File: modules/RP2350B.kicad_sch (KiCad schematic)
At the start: 34 parts, among them SW1 SW_Push, SW2 SW_Push, U1 RP2350B, U5 W25Q128JVS, U6 W25Q128JVS, Y1 12MHz

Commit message: Adding source, source control
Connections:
- net RP_NRESET: now reaches SW1.2, U1.35 (RUN)
- net RPB_CLK renamed RPB_SPI_CLK
- net RPB_MISO renamed RPB_SPI_MISO
- net RPB_MOSI renamed RPB_SPI_MOSI
- net RPB_SS renamed RPB_SPI_SS
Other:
- moved on the sheet: R7, SW1
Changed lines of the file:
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@@
 	(wire
 		(pts
-			(xy 64.77 130.81) (xy 64.77 132.08)
+			(xy 58.42 130.81) (xy 58.42 132.08)
 		)
 		(stroke
@@
 	(wire
 		(pts
-			(xy 88.9 130.81) (xy 100.33 130.81)
+			(xy 82.55 130.81) (xy 100.33 130.81)
 		)
 		(stroke
@@
 	(wire
 		(pts
-			(xy 71.12 130.81) (xy 64.77 130.81)
+			(xy 64.77 130.81) (xy 58.42 130.81)
 		)
 		(stroke
@@
 		)
 	)
+	(label "RP_NRESET"
+		(at 83.82 130.81 0)
+		(effects
+			(font
+				(size 1.27 1.27)
+			)
+			(justify left bottom)
+		)
+	)
 	(label "QSPI_SD2"
 		(at 210.82 132.08 0)
@@
 		)
 	)
+	(hierarchical_label "RPB_SWO"
+		(shape output)
+		(at 38.1 179.07 0)
+		(effects
+			(font
+				(size 1.27 1.27)
+			)
+			(justify left)
+		)
+	)
 	(hierarchical_label "USB_DM"
 		(shape input)
@@
 		)
 	)
-	(hierarchical_label "RPB_CLK"
+	(hierarchical_label "RPB_SPI_CLK"
 		(shape output)
 		(at 160.02 69.85 0)
@@
 		)
 	)
-	(hierarchical_label "RPB_SS"
+	(hierarchical_label "RPB_SPI_SS"
 		(shape output)
 		(at 160.02 72.39 0)
@@
 		)
 	)
-	(hierarchical_label "RPB_MOSI"
+	(hierarchical_label "RPB_SPI_MOSI"
 		(shape input)
 		(at 160.02 67.31 0)
@@
 		)
 	)
-	(hierarchical_label "RPB_MISO"
+	(hierarchical_label "RPB_SPI_MISO"
 		(shape output)
 		(at 160.02 64.77 0)
@@
 		)
 	)
+	(hierarchical_label "RPB_I2C_SDA"
+		(shape output)
+		(at 38.1 182.88 0)
+		(effects
+			(font
+				(size 1.27 1.27)
+			)
+			(justify left)
+		)
+	)
+	(hierarchical_label "RPB_I2C_SCL"
+		(shape output)
+		(at 38.1 186.69 0)
+		(effects
+			(font
+				(size 1.27 1.27)
+			)
+			(justify left)
+		)
+	)
 	(symbol
 		(lib_id "Device:C")
@@
 	(symbol
 		(lib_id "power:GND")
-		(at 64.77 132.08 0)
+		(at 58.42 132.08 0)
 		(unit 1)
 		(exclude_from_sim no)
@@
 		(fields_autoplaced yes)
 		(property "Reference" "#PWR018"
-			(at 64.77 138.43 0)
+			(at 58.42 138.43 0)
 			(effects
 				(font
@@
 		)
 		(property "Value" "GND"
-			(at 64.77 137.16 0)
+			(at 58.42 137.16 0)
 			(effects
 				(font
@@
 		)
 		(property "Footprint" ""
-			(at 64.77 132.08 0)
+			(at 58.42 132.08 0)
 			(effects
 				(font
@@
 		)
 		(property "Datasheet" ""
-			(at 64.77 132.08 0)
+			(at 58.42 132.08 0)
 			(effects
 				(font
@@
 		)
 		(property "Description" "Power symbol creates a global label with name \"GND\" , ground"
-			(at 64.77 132.08 0)
+			(at 58.42 132.08 0)
 			(effects
 				(font
@@
 	(symbol
 		(lib_id "Device:R")
-		(at 74.93 130.81 90)
+		(at 68.58 130.81 90)
 		(unit 1)
 		(exclude_from_sim no)
@@
 		(dnp no)
 		(property "Reference" "R7"
-			(at 74.93 128.778 90)
+			(at 68.58 128.778 90)
 			(effects
 				(font
@@
 		)
 		(property "Value" "1K"
-			(at 74.93 133.096 90)
+			(at 68.58 133.096 90)
 			(effects
 				(font
@@
 		)
 		(property "Footprint" "Resistor_SMD:R_0402_1005Metric"
-			(at 74.93 132.588 90)
+			(at 68.58 132.588 90)
 			(effects
 				(font
@@
 		)
 		(property "Datasheet" "https://industrial.panasonic.com/cdbs/www-data/pdf/RDA0000/AOA0000C304.pdf"
-			(at 74.93 130.81 0)
+			(at 68.58 130.81 0)
 			(effects
 				(font
@@
 		)
 		(property "Description" "RES SMD 1K OHM 1% 1/10W 0402"
-			(at 74.93 130.81 0)
+			(at 68.58 130.81 0)
 			(effects
 				(font
@@
 		)
 		(property "Part Number" "ERJ-2RKF1001X"
-			(at 74.93 130.81 90)
+			(at 68.58 130.81 90)
 			(effects
 				(font
@@
 		)
 		(property "Provider" "Digikey"
-			(at 74.93 130.81 90)
+			(at 68.58 130.81 90)
 			(effects
 				(font
@@
 	(symbol
 		(lib_id "Switch:SW_Push")
-		(at 83.82 130.81 0)
+		(at 77.47 130.81 0)
 		(unit 1)
 		(exclude_from_sim no)
@@
 		(fields_autoplaced yes)
 		(property "Reference" "SW1"
-			(at 83.82 123.19 0)
+			(at 77.47 123.19 0)
 			(effects
 				(font
@@
 		)
 		(property "Value" "SW_Push"
-			(at 83.82 125.73 0)
+			(at 77.47 125.73 0)
 			(effects
 				(font
@@
 		)
 		(property "Footprint" ""
-			(at 83.82 125.73 0)
+			(at 77.47 125.73 0)
 			(effects
 				(font
@@
 		)
 		(property "Datasheet" "~"
-			(at 83.82 125.73 0)
+			(at 77.47 125.73 0)
 			(effects
 				(font
@@
 		)
 		(property "Description" "Push button switch, generic, two pins"
-			(at 83.82 130.81 0)
+			(at 77.47 130.81 0)
 			(effects
 				(font

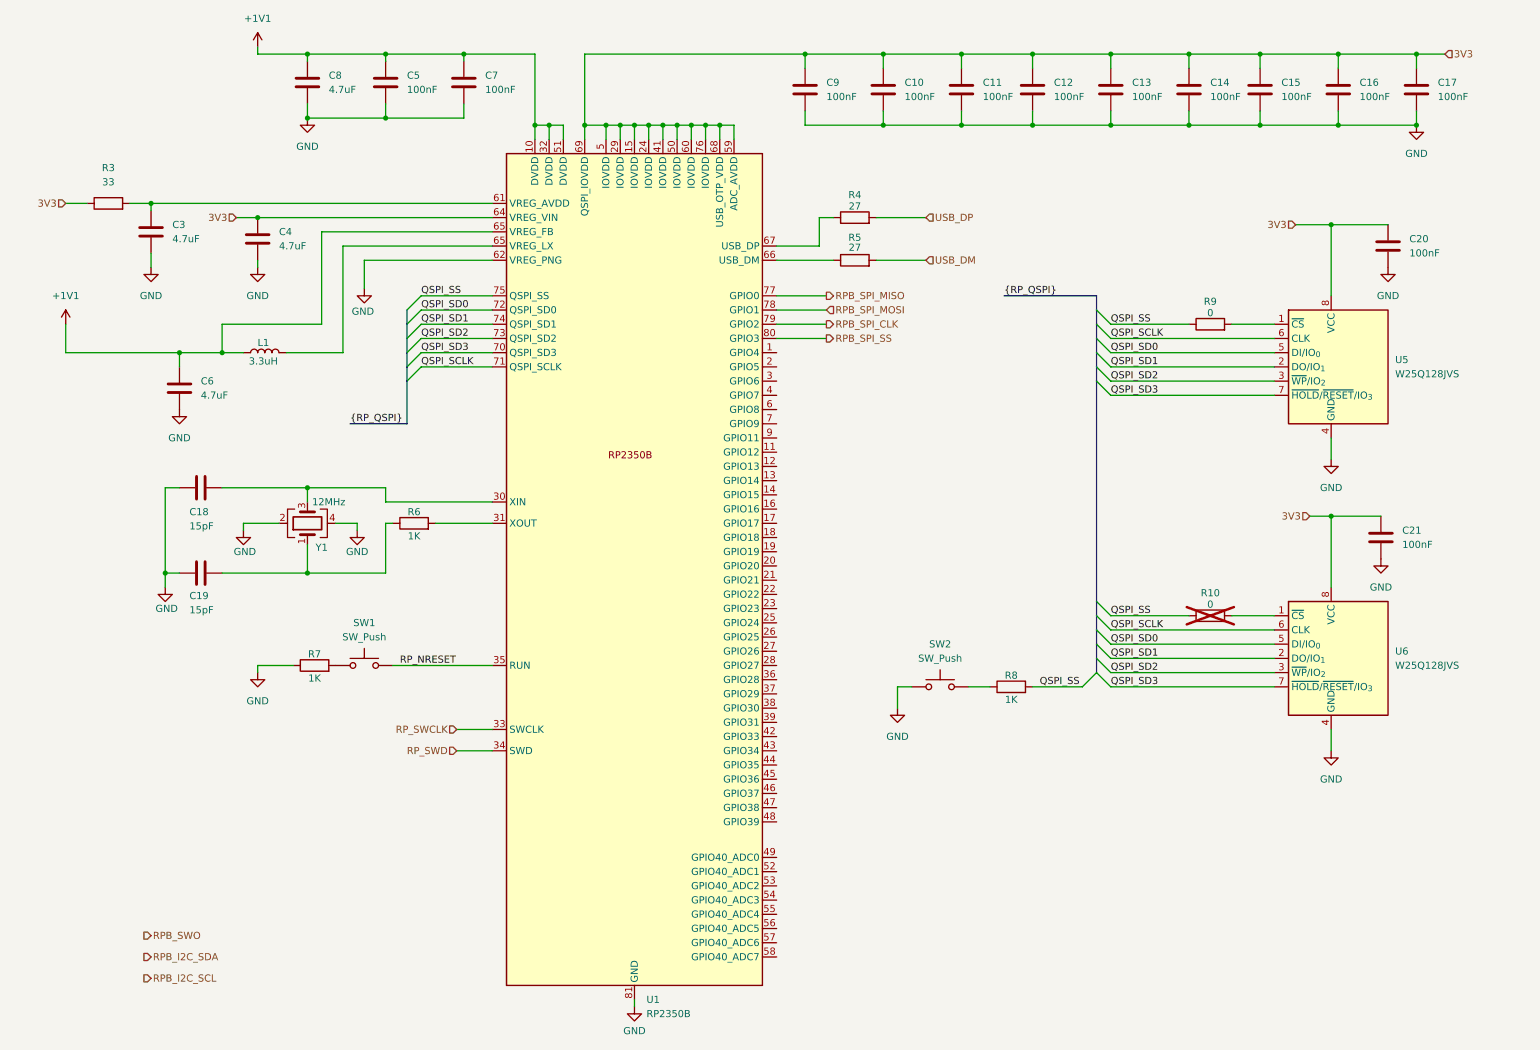
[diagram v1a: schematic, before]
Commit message: Modificaciond de conexiones
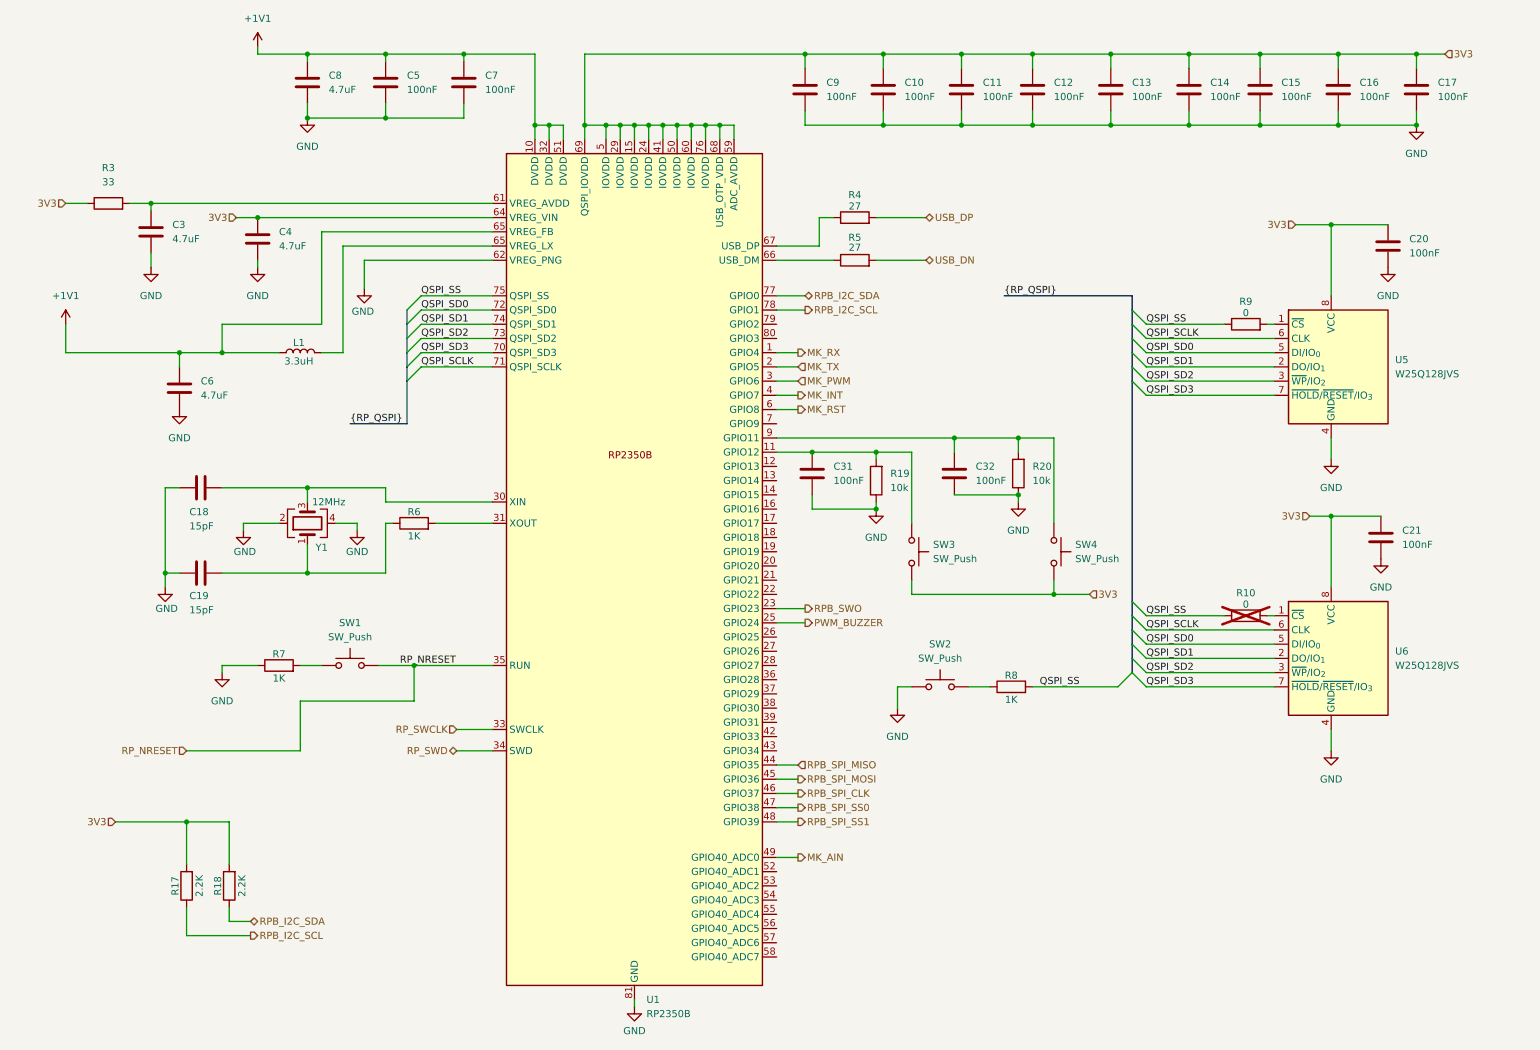
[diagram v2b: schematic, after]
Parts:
- added C31, C32: 100nF, Capacitor_SMD:C_0402_1005Metric, symbol Device:C
- added R17, R18: 2.2K, Resistor_SMD:R_0603_1608Metric, symbol Device:R
- added R19, R20: 10k, Resistor_SMD:R_0603_1608Metric, symbol Device:R
- added SW3, SW4: SW_Push, Button_Switch_SMD:SW_Push_1P1T_NO_Vertical_Wuerth_434133025816, symbol Switch:SW_Push
- C10, C11, C12, C13, C14, C15, C16, C17, C18, C19, C20, C21, C3, C4, C5, C6, C7, C8, C9: Provider (none) -> Digikey
- SW1, SW2: footprint (none) -> Button_Switch_SMD:SW_Push_1P1T_NO_Vertical_Wuerth_434133025816; Part Number (none) -> 434133025816; Provider (none) -> Digikey
- U1: Part Number (none) -> SC1510-A4; Provider (none) -> Digikey
- U5, U6: Part Number (none) -> W25Q128JVSIM TR; Provider (none) -> Digikey
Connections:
- net 3V3: now also R17.2, R18.2, SW3.2, SW4.2
- net GND: now also C31.2, C32.2, R19.1, R20.1
- net RPB_I2C_SCL: now also U1.78 (GPIO1), R17.1
- net RPB_I2C_SDA: now also U1.77 (GPIO0), R18.1
- net RPB_SPI_CLK: now also U1.46 (GPIO37); no longer U1.79 (GPIO2)
- net RPB_SPI_MISO: now also U1.44 (GPIO35); no longer U1.77 (GPIO0)
- net RPB_SPI_MOSI: now also U1.45 (GPIO36); no longer U1.78 (GPIO1)
- net RPB_SWO: now also U1.23 (GPIO23)
- net MK_RX: now reaches U1.1 (GPIO4)
- net at U1.11 (GPIO12): now also C31.1, R19.2, SW3.1
- net MK_TX: now reaches U1.2 (GPIO5)
- net PWM_BUZZER: now reaches U1.25 (GPIO24)
- net MK_PWM: now reaches U1.3 (GPIO6)
- net MK_INT: now reaches U1.4 (GPIO7)
- net RPB_SPI_SS0: now reaches U1.47 (GPIO38)
- net RPB_SPI_SS1: now reaches U1.48 (GPIO39)
- net MK_AIN: now reaches U1.49 (GPIO40_ADC0)
- net MK_RST: now reaches U1.6 (GPIO8)
- net at U1.9 (GPIO11): now also C32.1, R20.2, SW4.1
- net RPB_SPI_SS: no longer names the net of U1.80 (GPIO3)
- net USB_DM renamed USB_DN
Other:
- moved on the sheet: L1, R10, R7, R9

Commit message: correction of mikroBUS, USB on ESP32 and power mosfet
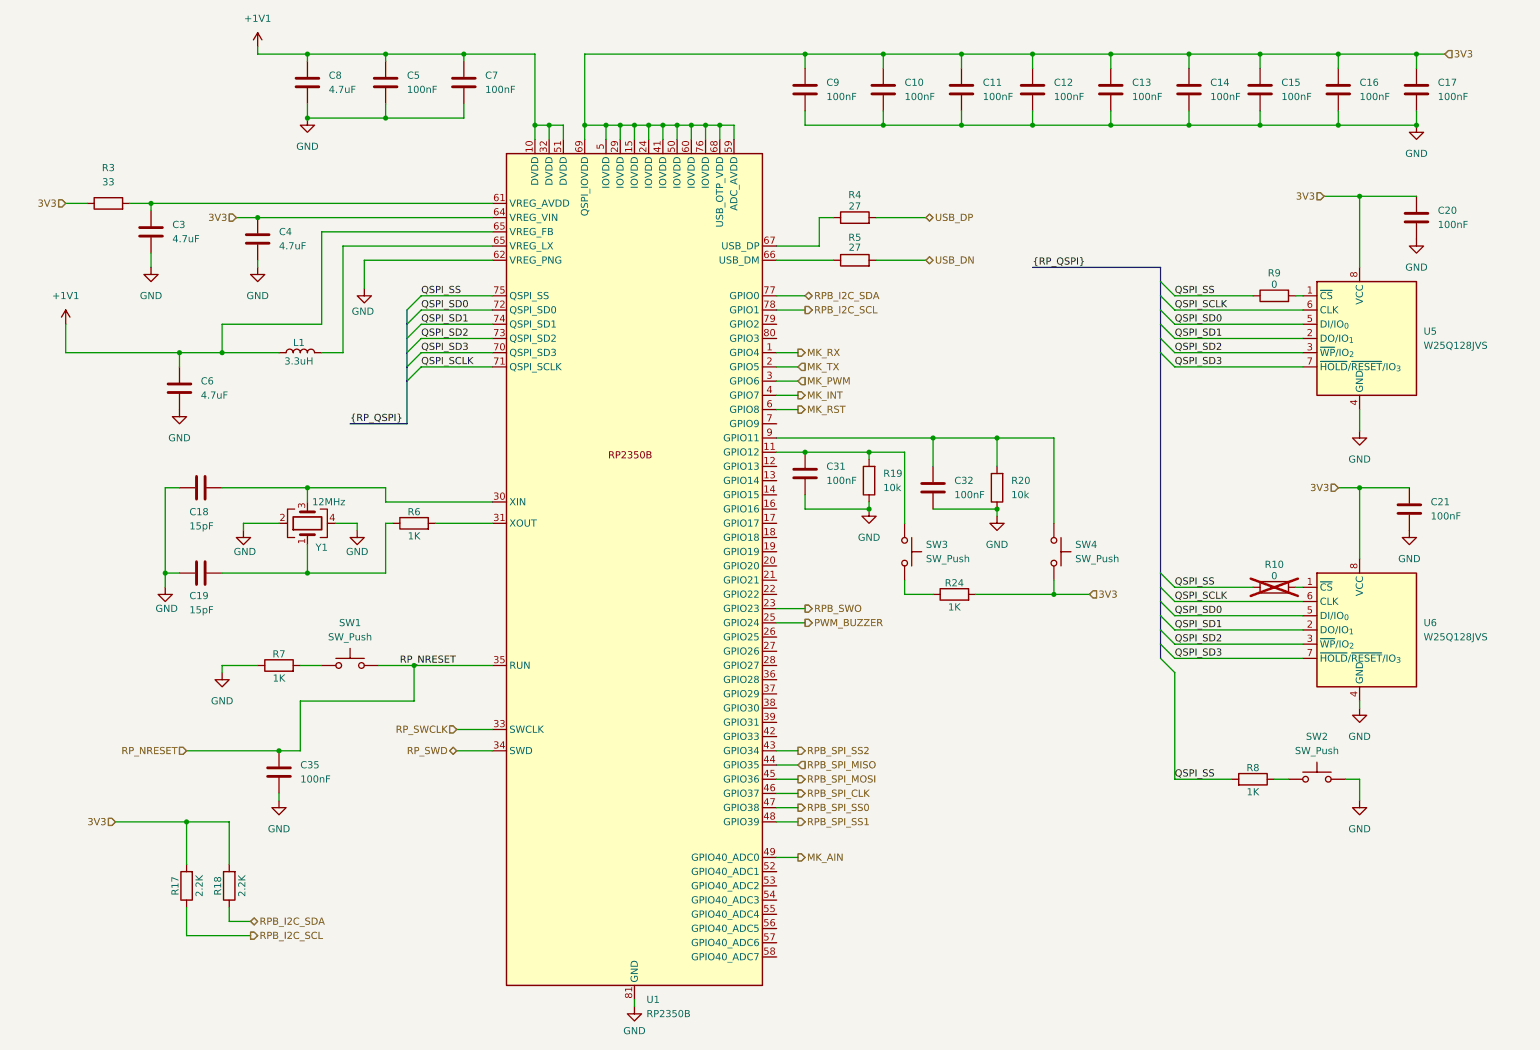
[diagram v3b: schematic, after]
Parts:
- added C35: 100nF, Capacitor_SMD:C_0402_1005Metric, symbol Device:C
- added R24: 1K, Resistor_SMD:R_0402_1005Metric, symbol Device:R
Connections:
- net 3V3: now also R24.2; no longer SW3.2
- net GND: now also C35.2
- net RP_NRESET: now also C35.1
- net RPB_SPI_SS2: now reaches U1.43 (GPIO34)
- new net: R24.1, SW3.2
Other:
- moved on the sheet: C20, C21, C31, C32, R10, R19, R20, R8, R9, SW2, SW3, U5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

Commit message: pcb power layout
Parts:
- added C37, C38: 100nF, Capacitor_SMD:C_0402_1005Metric, symbol Device:C
- C4, C6: footprint Capacitor_SMD:C_0402_1005Metric -> Capacitor_SMD:C_0603_1608Metric
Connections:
- net +1V1: now also C38.1
- net 3V3: now also C37.1
- net GND: now also C37.2, C38.2
- net USB_IN_P: now reaches R4.1, U1.67 (USB_DP)
- net USB_IN_N: now reaches R5.1, U1.66 (USB_DM)
- net VGREX_LX: now reaches L1.2
- net VGREX_LX: now also U1.63 (VREG_LX); no longer U1.65 (VREG_LX)
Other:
- moved on the sheet: C5, C7, C8, R4, R5

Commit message: save
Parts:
- removed C21: 100nF, Capacitor_SMD:C_0402_1005Metric, symbol Device:C
- removed R10, R9: 0, Resistor_SMD:R_0603_1608Metric, symbol Device:R
- removed SW2: SW_Push, Button_Switch_SMD:SW_Push_1P1T_NO_Vertical_Wuerth_434133025816, symbol Switch:SW_Push
- removed U6: W25Q128JVS, Package_SO:SOIC-8_5.3x5.3mm_P1.27mm, symbol Memory_Flash:W25Q128JVS
- added C39: 100nF, Capacitor_SMD:C_0402_1005Metric, symbol Device:C
- added TP18, TP21, TP22, TP23, TP24, TP25, TP6: TestPoint, TestPoint:TestPoint_THTPad_D1.0mm_Drill0.5mm, symbol Connector:TestPoint
- added TP19, TP20: TestPoint, TestPoint:TestPoint_Pad_D1.0mm, symbol Connector:TestPoint
- added TP5: TestPoint, TestPoint:TestPoint_THTPad_D1.5mm_Drill0.7mm, symbol Connector:TestPoint
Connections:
- net +1V1: now also TP5.1
- net 3V3: now also C39.1
- net GND: now also C39.2
- net QSPI_SCLK: now also TP21.1
- net QSPI_SD0: now also TP22.1
- net QSPI_SD1: now also TP23.1
- net QSPI_SD2: now also TP24.1
- net QSPI_SD3: now also TP25.1
- net QSPI_SS: now also U5.1 (~{CS}), TP18.1; no longer R8.2
- net at R8.1: now also SW4.1
- net at C32.1, R20.2, U1.9 (GPIO11): now also R8.2; no longer SW4.1
- net at C18.1, U1.30 (XIN), Y1.3: now also TP19.1
- net at C3.1, R3.2, U1.61 (VREG_AVDD): now also TP6.1
- net at C19.1, R6.1, Y1.1: now also TP20.1
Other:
- moved on the sheet: SW4

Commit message: Cambio de layout, correccion de pinout
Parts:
- removed C17, C32: 100nF, Capacitor_SMD:C_0402_1005Metric, symbol Device:C
- removed TP19, TP20: TestPoint, TestPoint:TestPoint_Pad_D1.0mm, symbol Connector:TestPoint
- removed TP6: TestPoint, TestPoint:TestPoint_THTPad_D1.0mm_Drill0.5mm, symbol Connector:TestPoint
- added C18: 100nF, Capacitor_SMD:C_0603_1608Metric, symbol Device:C
- added C39: 100nF, Capacitor_SMD:C_0402_1005Metric, symbol Device:C
- C16: renamed from C31; footprint Capacitor_SMD:C_0402_1005Metric -> Capacitor_SMD:C_0603_1608Metric
- C38: renamed from C20; footprint Capacitor_SMD:C_0402_1005Metric -> Capacitor_SMD:C_0603_1608Metric
- C9: renamed from C35; footprint Capacitor_SMD:C_0402_1005Metric -> Capacitor_SMD:C_0603_1608Metric
- R18: renamed from R24; footprint Resistor_SMD:R_0402_1005Metric -> Resistor_SMD:R_0603_1608Metric
- R20: renamed from R8; footprint Resistor_SMD:R_0402_1005Metric -> Capacitor_SMD:C_0603_1608Metric
- R6: renamed from R7; footprint Resistor_SMD:R_0402_1005Metric -> Resistor_SMD:R_0603_1608Metric
- TP18, TP21, TP22, TP23, TP24, TP25: footprint TestPoint:TestPoint_THTPad_D1.0mm_Drill0.5mm -> Sadman_TP:TP_2.8mm_1mm
- TP5: footprint TestPoint:TestPoint_THTPad_D1.5mm_Drill0.7mm -> Sadman_TP:TP_2.8mm_1mm
- renumbered C5 to C10, C7 to C11, C38 to C12, C39 to C13, C37 to C14, C9 to C15, C10 to C17, C11 to C19, C12 to C20, C13 to C28, C14 to C31, C15 to C32, C16 to C35, C6 to C4, C18 to C5, C19 to C6, C8 to C7, C4 to C8, R4 to R12, R5 to R17, R20 to R19, R17 to R4, R18 to R5, R6 to R7, R19 to R8
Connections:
- net 3V3: now also R20.1, C39.1; no longer SW4.2
- net GND: now also C18.2, C39.2
- net MK_INT: now also U1.43 (GPIO34); no longer U1.4 (GPIO7)
- net MK_PWM: now also U1.42 (GPIO33); no longer U1.3 (GPIO6)
- net MK_RST: now also U1.53 (GPIO40_ADC2); no longer U1.6 (GPIO8)
- net MK_RX: now also U1.45 (GPIO36); no longer U1.1 (GPIO4)
- net MK_TX: now also U1.46 (GPIO37); no longer U1.2 (GPIO5)
- net PWM_BUZZER: now also U1.80 (GPIO3); no longer U1.25 (GPIO24)
- net RPB_SPI_CLK: now also U1.38 (GPIO30); no longer U1.46 (GPIO37)
- net RPB_SPI_MISO: now also U1.37 (GPIO29); no longer U1.44 (GPIO35)
- net RPB_SPI_MOSI: now also U1.36 (GPIO28); no longer U1.45 (GPIO36)
- net RPB_SPI_SS0: now also U1.39 (GPIO31); no longer U1.47 (GPIO38)
- net RPB_SPI_SS1: now also U1.44 (GPIO35); no longer U1.48 (GPIO39)
- net RPB_SPI_SS2: now also U1.1 (GPIO4); no longer U1.43 (GPIO34)
- net RPB_SWO: no longer U1.23 (GPIO23)
- net at C16.1, R8.2, SW3.1: now also U1.14 (GPIO15); no longer U1.11 (GPIO12)
- net RP_XIN: now reaches C5.1, U1.30 (XIN), Y1.3
- net VGREX_AVDD: now reaches C3.1, R3.2, U1.61 (VREG_AVDD)
- net RP_XOUT: now reaches R7.2, U1.31 (XOUT)
- net at U1.13 (GPIO14): now also R19.2, SW4.1, C18.1
- net MK_AIN2: now reaches U1.54 (GPIO40_ADC3)
- net MK_PWM2: now reaches U1.55 (GPIO40_ADC4)
- net MK_INT2: now reaches U1.56 (GPIO40_ADC5)
- net MK_RX2: now reaches U1.57 (GPIO40_ADC6)
- net MK_TX2: now reaches U1.58 (GPIO40_ADC7)
- new net: R20.2, SW4.2
- new net MK_RST2: U1.47 (GPIO38)
- now unconnected: U1.9 (GPIO11)
- no-connect marks 0 -> 1
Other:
- moved on the sheet: C10, C11, C12, C13, C14, C15, C16, C17, C19, C20, C28, C3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
